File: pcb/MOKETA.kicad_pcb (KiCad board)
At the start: 2 copper layers, 286.8 x 115.6 mm, 140 parts, among them SW43 Reset, U1 Pro_Micro

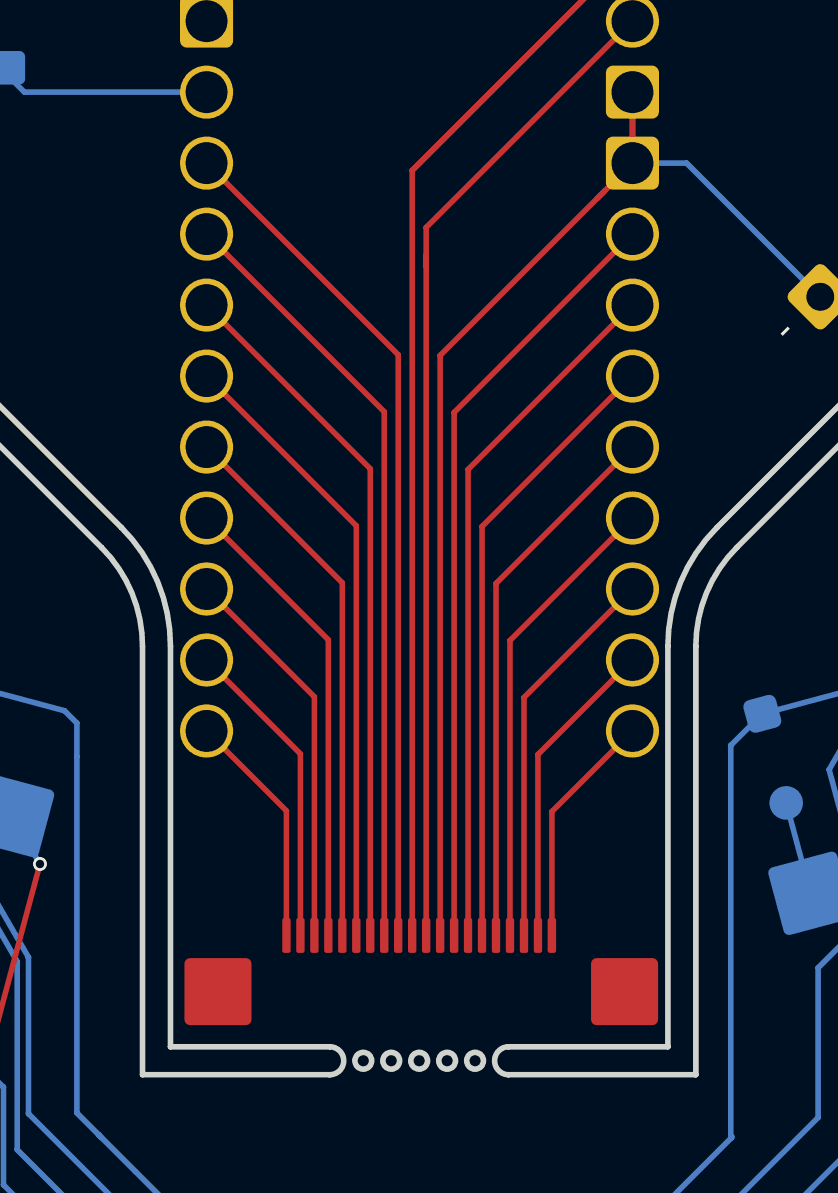
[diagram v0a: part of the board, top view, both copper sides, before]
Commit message: Connector on doter rotated 180 degree
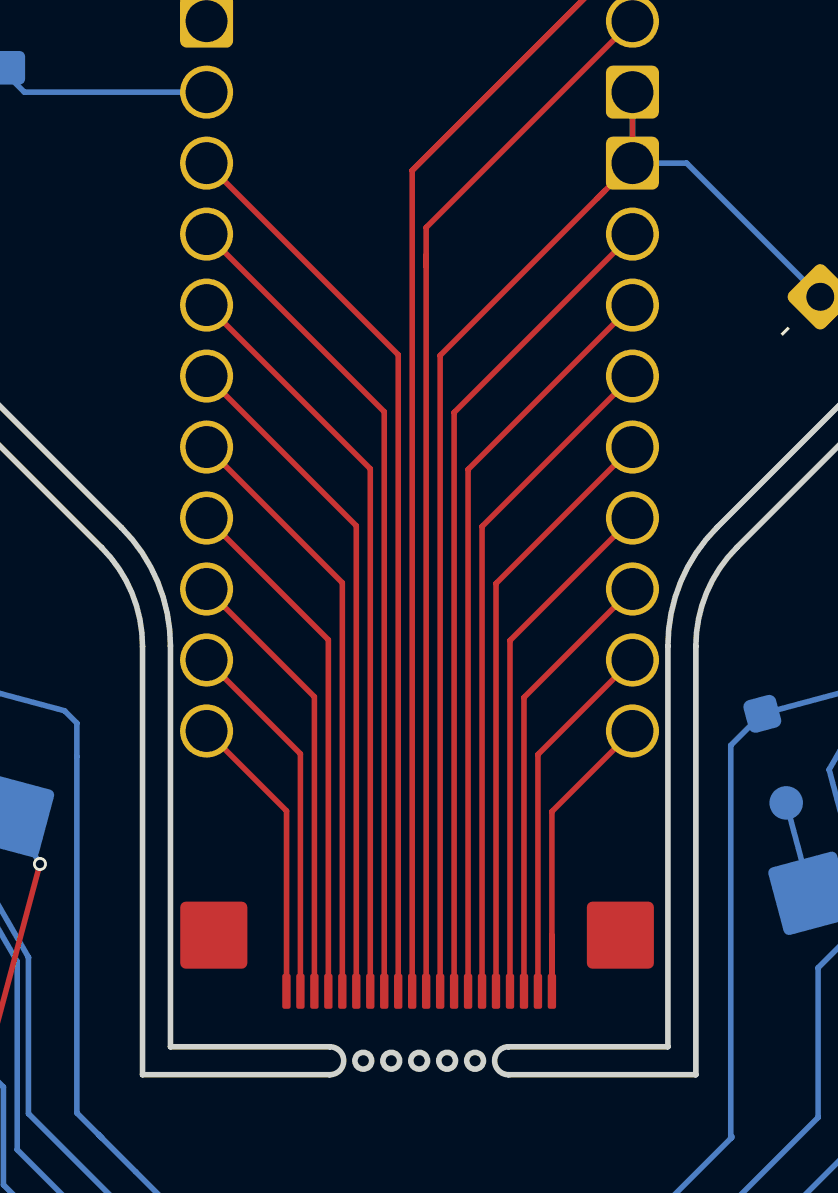
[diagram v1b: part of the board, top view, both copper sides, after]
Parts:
- moved J3 4.00 mm to (203.2, 129.9), turned to 180 degrees
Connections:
- J3 pad 1: R6D -> LED3D
- J3 pad 10: LEDSD -> LED1D
- J3 pad 11: LED1D -> LEDSD
- J3 pad 12: GNDD -> VCCD
- J3 pad 13: R0D -> R1D
- J3 pad 14: R2D -> R3D
- J3 pad 15: R4D -> R5D
- J3 pad 16: C0D -> C3D
- J3 pad 17: C1D -> C4D
- J3 pad 18: C2D -> C5D
- J3 pad 19: LED2D -> LED4D
- J3 pad 2: LED4D -> LED2D
- J3 pad 20: LED3D -> R6D
- J3 pad 3: C5D -> C2D
- J3 pad 4: C4D -> C1D
- J3 pad 5: C3D -> C0D
- J3 pad 6: R5D -> R4D
- J3 pad 7: R3D -> R2D
- J3 pad 8: R1D -> R0D
- J3 pad 9: VCCD -> GNDD
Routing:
- net LED3D: track 8.51 -> 12.5 mm
- net R6D: track 8.50 -> 10.5 mm
- net LED1D: track 36.2 -> 38.2 mm
- net R3D: track 25.0 -> 27.0 mm
- net C1D: track 16.7 -> 18.7 mm
- net R4D: track 22.2 -> 24.2 mm
- net GNDD: track 39.6 -> 41.6 mm
- net C3D: track 19.5 -> 21.5 mm
- net LEDSD: track 48.3 -> 50.3 mm
- net C0D: track 19.5 -> 21.5 mm
- net R0D: track 27.7 -> 29.7 mm
- net R1D: track 27.7 -> 29.7 mm
- net VCCD: track 30.5 -> 32.5 mm
- net R2D: track 25.0 -> 27.0 mm
- net LED2D: track 11.3 -> 13.3 mm
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
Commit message: No separate doter, flex PCB instead
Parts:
- removed J2, J3: ~, moketa:FFC_CMD_1x20_P0.5mm
- added MH: Untitled, moketa:M2 Hole, F.Cu at (179.7, 94.9)
- added MH: Untitled, moketa:M2 Hole, F.Cu at (268.6, 158.4)
- added MH: Untitled, moketa:M2 Hole, F.Cu at (137.7, 158.4)
- added MH: Untitled, moketa:M2 Hole, F.Cu at (226.7, 94.9)
- moved J1 77.9 mm to (203.2, 182.4), turned to 0 degrees
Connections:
- D1 pad 1: R0P -> R0
- D10 pad 1: R1P -> R1
- D11 pad 1: R1P -> R1
- D12 pad 1: R1P -> R1
- D13 pad 1: R2P -> R2
- D14 pad 1: R2P -> R2
- D15 pad 1: R2P -> R2
- D16 pad 1: R2P -> R2
- D17 pad 1: R2P -> R2
- D18 pad 1: R2P -> R2
- D19 pad 1: R3P -> R3
- D2 pad 1: R0P -> R0
- D20 pad 1: R3P -> R3
- D21 pad 1: R3P -> R3
- D22 pad 1: R3P -> R3
- D23 pad 1: R3P -> R3
- D24 pad 1: R3P -> R3
- D25 pad 1: R4P -> R4
- D26 pad 1: R4P -> R4
- D27 pad 1: R4P -> R4
- D28 pad 1: R4P -> R4
- D29 pad 1: R4P -> R4
- D3 pad 1: R0P -> R0
- D30 pad 1: R4P -> R4
- D31 pad 1: R5P -> R5
- D32 pad 1: R5P -> R5
- D33 pad 1: R5P -> R5
- D34 pad 1: R5P -> R5
- D35 pad 1: R5P -> R5
- D36 pad 1: R5P -> R5
- D37 pad 1: R6P -> R6
- D38 pad 1: R6P -> R6
- D39 pad 1: R6P -> R6
- D4 pad 1: R0P -> R0
- D40 pad 1: R6P -> R6
- D41 pad 1: R6P -> R6
- D42 pad 1: R6P -> R6
- D43 pad 1: GNDP -> GND
- D44 pad 1: GNDP -> GND
- D45 pad 1: GNDP -> GND
- D46 pad 1: GNDP -> GND
- D5 pad 1: R0P -> R0
- D6 pad 1: R0P -> R0
- D7 pad 1: R1P -> R1
- D8 pad 1: R1P -> R1
- D9 pad 1: R1P -> R1
- J1 pad 2: GNDD -> GND
- LED1 pad 1: VCCP -> VCC
- LED1 pad 3: GNDP -> GND
- LED10 pad 1: VCCP -> VCC
- LED10 pad 3: GNDP -> GND
- LED11 pad 1: VCCP -> VCC
- LED11 pad 3: GNDP -> GND
- LED12 pad 1: VCCP -> VCC
- LED12 pad 3: GNDP -> GND
- LED13 pad 1: VCCP -> VCC
- LED13 pad 3: GNDP -> GND
- LED14 pad 1: VCCP -> VCC
- LED14 pad 3: GNDP -> GND
- LED15 pad 1: VCCP -> VCC
- LED15 pad 3: GNDP -> GND
- LED16 pad 1: VCCP -> VCC
- LED16 pad 3: GNDP -> GND
- LED17 pad 1: VCCP -> VCC
- LED17 pad 3: GNDP -> GND
- LED18 pad 1: VCCP -> VCC
- LED18 pad 3: GNDP -> GND
- LED19 pad 1: VCCP -> VCC
- LED19 pad 3: GNDP -> GND
- LED2 pad 1: VCCP -> VCC
- LED2 pad 3: GNDP -> GND
- LED20 pad 1: VCCP -> VCC
- LED20 pad 3: GNDP -> GND
- LED21 pad 1: VCCP -> VCC
- LED21 pad 3: GNDP -> GND
- LED22 pad 1: VCCP -> VCC
- LED22 pad 3: GNDP -> GND
- LED23 pad 1: VCCP -> VCC
- LED23 pad 3: GNDP -> GND
- LED24 pad 1: VCCP -> VCC
- LED24 pad 3: GNDP -> GND
- LED25 pad 1: VCCP -> VCC
- LED25 pad 3: GNDP -> GND
- LED26 pad 1: VCCP -> VCC
- LED26 pad 3: GNDP -> GND
- LED27 pad 1: VCCP -> VCC
- LED27 pad 3: GNDP -> GND
- LED28 pad 1: VCCP -> VCC
- LED28 pad 3: GNDP -> GND
- LED29 pad 1: VCCP -> VCC
- LED29 pad 3: GNDP -> GND
- LED3 pad 1: VCCP -> VCC
- LED3 pad 3: GNDP -> GND
- LED30 pad 1: VCCP -> VCC
- LED30 pad 3: GNDP -> GND
- LED31 pad 1: VCCP -> VCC
- LED31 pad 3: GNDP -> GND
- LED32 pad 1: VCCP -> VCC
- LED32 pad 3: GNDP -> GND
- LED33 pad 1: VCCP -> VCC
- LED33 pad 3: GNDP -> GND
- LED34 pad 1: VCCP -> VCC
- LED34 pad 3: GNDP -> GND
- LED35 pad 1: VCCP -> VCC
- LED35 pad 3: GNDP -> GND
- LED36 pad 1: VCCP -> VCC
- LED36 pad 3: GNDP -> GND
- LED37 pad 1: VCCP -> VCC
- LED37 pad 3: GNDP -> GND
- LED38 pad 1: VCCP -> VCC
- LED38 pad 3: GNDP -> GND
- LED39 pad 1: VCCP -> VCC
- LED39 pad 3: GNDP -> GND
- LED4 pad 1: VCCP -> VCC
- LED4 pad 3: GNDP -> GND
- LED40 pad 1: VCCP -> VCC
- LED40 pad 3: GNDP -> GND
- LED41 pad 1: VCCP -> VCC
- LED41 pad 3: GNDP -> GND
- LED42 pad 1: VCCP -> VCC
- LED42 pad 3: GNDP -> GND
- LED5 pad 1: VCCP -> VCC
- LED5 pad 3: GNDP -> GND
- LED6 pad 1: VCCP -> VCC
- LED6 pad 3: GNDP -> GND
- LED6 pad 4: LEDSP -> LEDS
- LED7 pad 1: VCCP -> VCC
- LED7 pad 3: GNDP -> GND
- LED8 pad 1: VCCP -> VCC
- LED8 pad 3: GNDP -> GND
- LED9 pad 1: VCCP -> VCC
- LED9 pad 3: GNDP -> GND
- R1 pad 1: LED1P -> LED1
- R2 pad 1: LED2P -> LED2
- R3 pad 1: LED3P -> LED3
- R4 pad 1: LED4P -> LED4
- SW1 pad 1: C0P -> C0
- SW10 pad 1: C3P -> C3
- SW11 pad 1: C4P -> C4
- SW12 pad 1: C5P -> C5
- SW13 pad 1: C0P -> C0
- SW14 pad 1: C1P -> C1
- SW15 pad 1: C2P -> C2
- SW16 pad 1: C3P -> C3
- SW17 pad 1: C4P -> C4
- SW18 pad 1: C5P -> C5
- SW19 pad 1: C0P -> C0
- SW2 pad 1: C1P -> C1
- SW20 pad 1: C1P -> C1
- SW21 pad 1: C2P -> C2
- SW22 pad 1: C3P -> C3
- SW23 pad 1: C4P -> C4
- SW24 pad 1: C5P -> C5
- SW25 pad 1: C0P -> C0
- SW26 pad 1: C1P -> C1
- SW27 pad 1: C2P -> C2
- SW28 pad 1: C3P -> C3
- SW29 pad 1: C4P -> C4
- SW3 pad 1: C2P -> C2
- SW30 pad 1: C5P -> C5
- SW31 pad 1: C0P -> C0
- SW32 pad 1: C1P -> C1
- SW33 pad 1: C2P -> C2
- SW34 pad 1: C3P -> C3
- SW35 pad 1: C4P -> C4
- SW36 pad 1: C5P -> C5
- SW37 pad 1: C3P -> C3
- SW38 pad 1: C4P -> C4
- SW39 pad 1: C5P -> C5
- SW4 pad 1: C3P -> C3
- SW40 pad 1: C0P -> C0
- SW41 pad 1: C1P -> C1
- SW42 pad 1: C2P -> C2
- SW5 pad 1: C4P -> C4
- SW6 pad 1: C5P -> C5
- SW7 pad 1: C0P -> C0
- SW8 pad 1: C1P -> C1
- SW9 pad 1: C2P -> C2
- U1 pad 1: LEDSD -> LEDS
- U1 pad 10: C2D -> C2
- U1 pad 11: LED2D -> LED2
- U1 pad 12: LED3D -> LED3
- U1 pad 13: R6D -> R6
- U1 pad 14: LED4D -> LED4
- U1 pad 15: C5D -> C5
- U1 pad 16: C4D -> C4
- U1 pad 17: C3D -> C3
- U1 pad 18: R5D -> R5
- U1 pad 19: R3D -> R3
- U1 pad 2: LED1D -> LED1
- U1 pad 20: R1D -> R1
- U1 pad 21: VCCD -> VCC
- U1 pad 3: GNDD -> GND
- U1 pad 4: GNDD -> GND
- U1 pad 5: R0D -> R0
- U1 pad 6: R2D -> R2
- U1 pad 7: R4D -> R4
- U1 pad 8: C0D -> C0
- U1 pad 9: C1D -> C1
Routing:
- net VCC: track 0.00 -> 1211.3 mm, vias 0 -> 1
- net VCCP: track 1178.2 -> 0.00 mm, vias 1 -> 0
- net C0: track 0.00 -> 371.7 mm, vias 0 -> 9
- net C1: track 0.00 -> 364.2 mm, vias 0 -> 8
- net C3: track 0.00 -> 354.1 mm, vias 0 -> 8
- net C0P: track 353.7 -> 0.00 mm, vias 9 -> 0
- net C2: track 0.00 -> 351.2 mm, vias 0 -> 9
- net C1P: track 347.0 -> 0.00 mm, vias 8 -> 0
- net C4: track 0.00 -> 339.1 mm, vias 0 -> 9
- net C5: track 0.00 -> 332.4 mm, vias 0 -> 8
- net C2P: track 326.8 -> 0.00 mm, vias 9 -> 0
- net C3P: track 322.2 -> 0.00 mm, vias 8 -> 0
- net C4P: track 304.5 -> 0.00 mm, vias 9 -> 0
- net C5P: track 298.8 -> 0.00 mm, vias 8 -> 0
- net R2: track 0.00 -> 218.2 mm, vias 0 -> 1
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- added copper zone on B.Cu, net GND
- added copper zone on F.Cu, net GND
- removed copper zone on B.Cu, net GNDP
- removed copper zone on F.Cu, net GNDP
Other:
- outline, holes or cut-outs redrawn

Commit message: Add another 2 holes on controller zone
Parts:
- added MH: Untitled, moketa:M2 Hole, F.Cu at (190.7, 105.8)
- added MH: Untitled, moketa:M2 Hole, F.Cu at (215.7, 105.9)
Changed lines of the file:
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@@
 		)
 	)
+	(footprint "moketa:M2 Hole"
+		(layer "F.Cu")
+		(at 190.721372 105.849998)
+		(property "Reference" "MH"
+			(at 0 -0.5 0)
+			(unlocked yes)
+			(layer "F.SilkS")
+			(hide yes)
+			(effects
+				(font
+					(size 1 1)
+					(thickness 0.1)
+				)
+			)
+		)
+		(property "Value" "Untitled"
+			(at 0 1 0)
+			(unlocked yes)
+			(layer "F.Fab")
+			(hide yes)
+			(effects
+				(font
+					(size 1 1)
+					(thickness 0.15)
+				)
+			)
+		)
+		(property "Datasheet" ""
+			(at 0 0 0)
+			(unlocked yes)
+			(layer "F.Fab")
+			(hide yes)
+			(effects
+				(font
+					(size 1 1)
+					(thickness 0.15)
+				)
+			)
+		)
+		(property "Description" ""
+			(at 0 0 0)
+			(unlocked yes)
+			(layer "F.Fab")
+			(hide yes)
+			(effects
+				(font
+					(size 1 1)
+					(thickness 0.15)
+				)
+			)
+		)
+		(attr smd)
+		(pad "" thru_hole circle
+			(at 0 0 180)
+			(size 3.5 3.5)
+			(drill 2.2)
+			(layers "*.Cu" "*.Paste" "*.Mask")
+			(remove_unused_layers no)
+		)
+		(embedded_fonts no)
+	)
 	(footprint "moketa:YS-SK6812MINI-E"
 		(layer "F.Cu")
@@
 		)
 	)
+	(footprint "moketa:M2 Hole"
+		(layer "F.Cu")
+		(at 215.67009 105.880245)
+		(property "Reference" "MH"
+			(at 0 -0.5 0)
+			(unlocked yes)
+			(layer "F.SilkS")
+			(hide yes)
+			(effects
+				(font
+					(size 1 1)
+					(thickness 0.1)
+				)
+			)
+		)
+		(property "Value" "Untitled"
+			(at 0 1 0)
+			(unlocked yes)
+			(layer "F.Fab")
+			(hide yes)
+			(effects
+				(font
+					(size 1 1)
+					(thickness 0.15)
+				)
+			)
+		)
+		(property "Datasheet" ""
+			(at 0 0 0)
+			(unlocked yes)
+			(layer "F.Fab")
+			(hide yes)
+			(effects
+				(font
+					(size 1 1)
+					(thickness 0.15)
+				)
+			)
+		)
+		(property "Description" ""
+			(at 0 0 0)
+			(unlocked yes)
+			(layer "F.Fab")
+			(hide yes)
+			(effects
+				(font
+					(size 1 1)
+					(thickness 0.15)
+				)
+			)
+		)
+		(attr smd)
+		(pad "" thru_hole circle
+			(at 0 0 180)
+			(size 3.5 3.5)
+			(drill 2.2)
+			(layers "*.Cu" "*.Paste" "*.Mask")
+			(remove_unused_layers no)
+		)
+		(embedded_fonts no)
+	)
 	(footprint "moketa:D_SOD-123"
 		(layer "F.Cu")
@@
 	)
 	(segment
-		(start 197.79604 93.45)
-		(end 195.588193 95.657847)
+		(start 213.15 93.25)
+		(end 197.99604 93.25)
 		(width 0.4)
 		(layer "B.Cu")
@@
 	)
 	(segment
-		(start 218.14573 95.215125)
-		(end 215.115125 95.215125)
+		(start 197.99604 93.25)
+		(end 195.588193 95.657847)
 		(width 0.4)
 		(layer "B.Cu")
@@
 	)
 	(segment
-		(start 213.35 93.45)
-		(end 197.79604 93.45)
+		(start 215.115125 95.215125)
+		(end 213.15 93.25)
 		(width 0.4)
 		(layer "B.Cu")
@@
 	)
 	(segment
-		(start 215.115125 95.215125)
-		(end 213.35 93.45)
+		(start 218.14573 95.215125)
+		(end 215.115125 95.215125)
 		(width 0.4)
 		(layer "B.Cu")
